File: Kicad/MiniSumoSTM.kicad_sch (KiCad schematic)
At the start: 0 parts

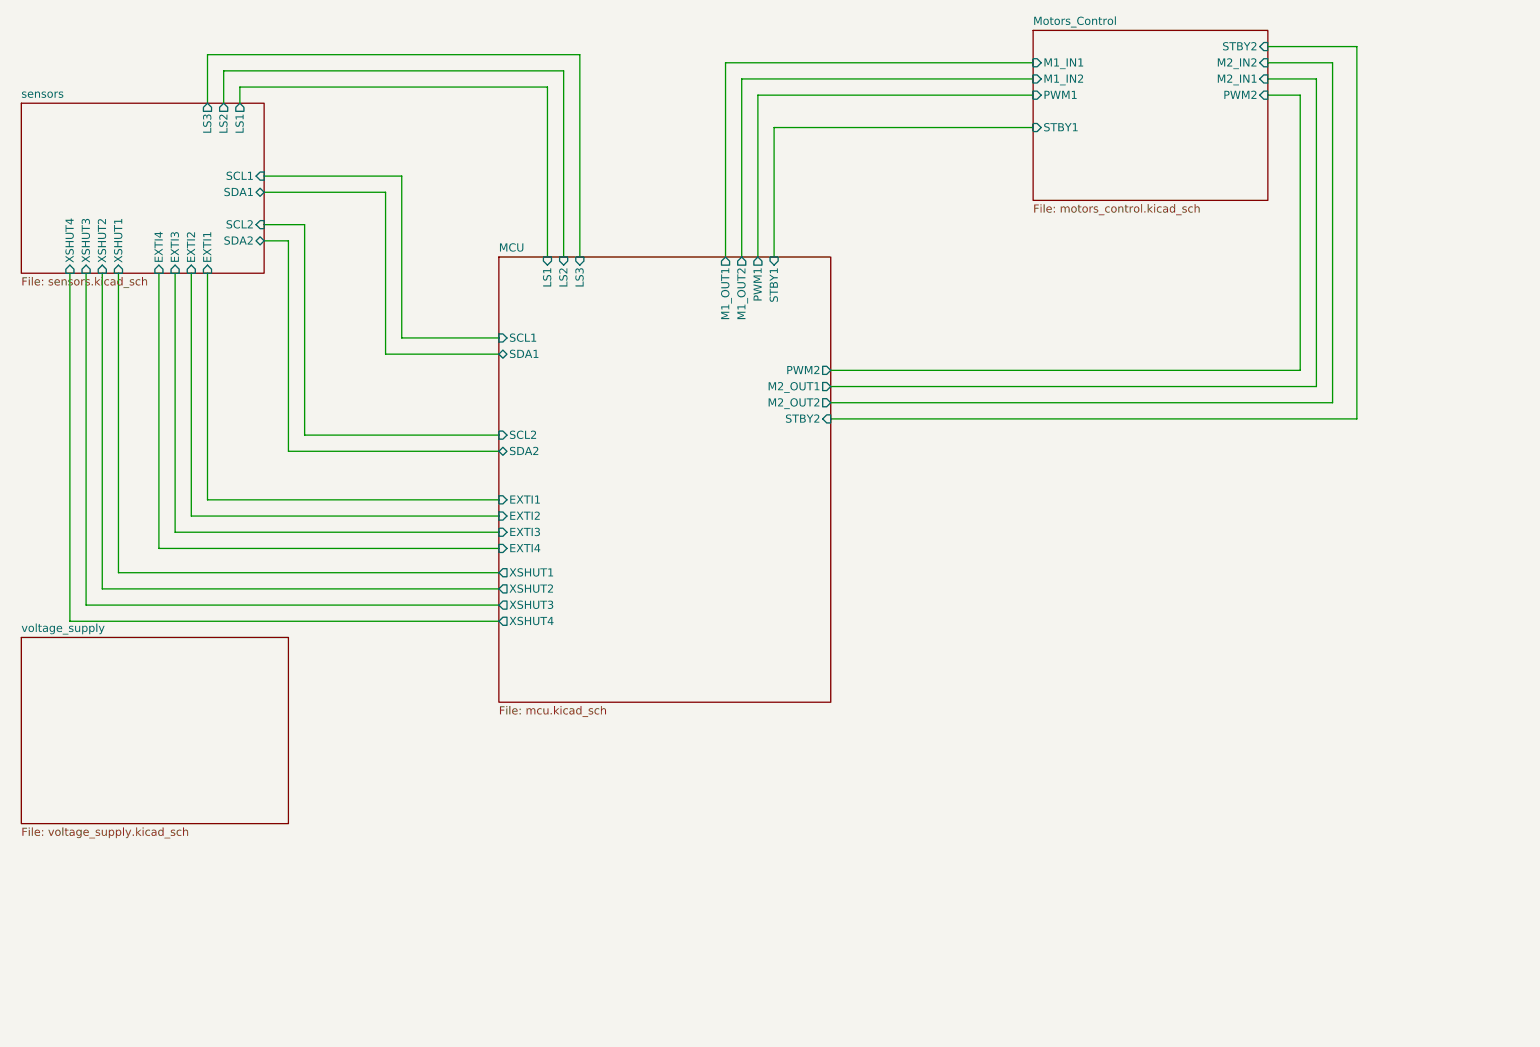
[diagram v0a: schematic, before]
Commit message: kicad schemas documentation
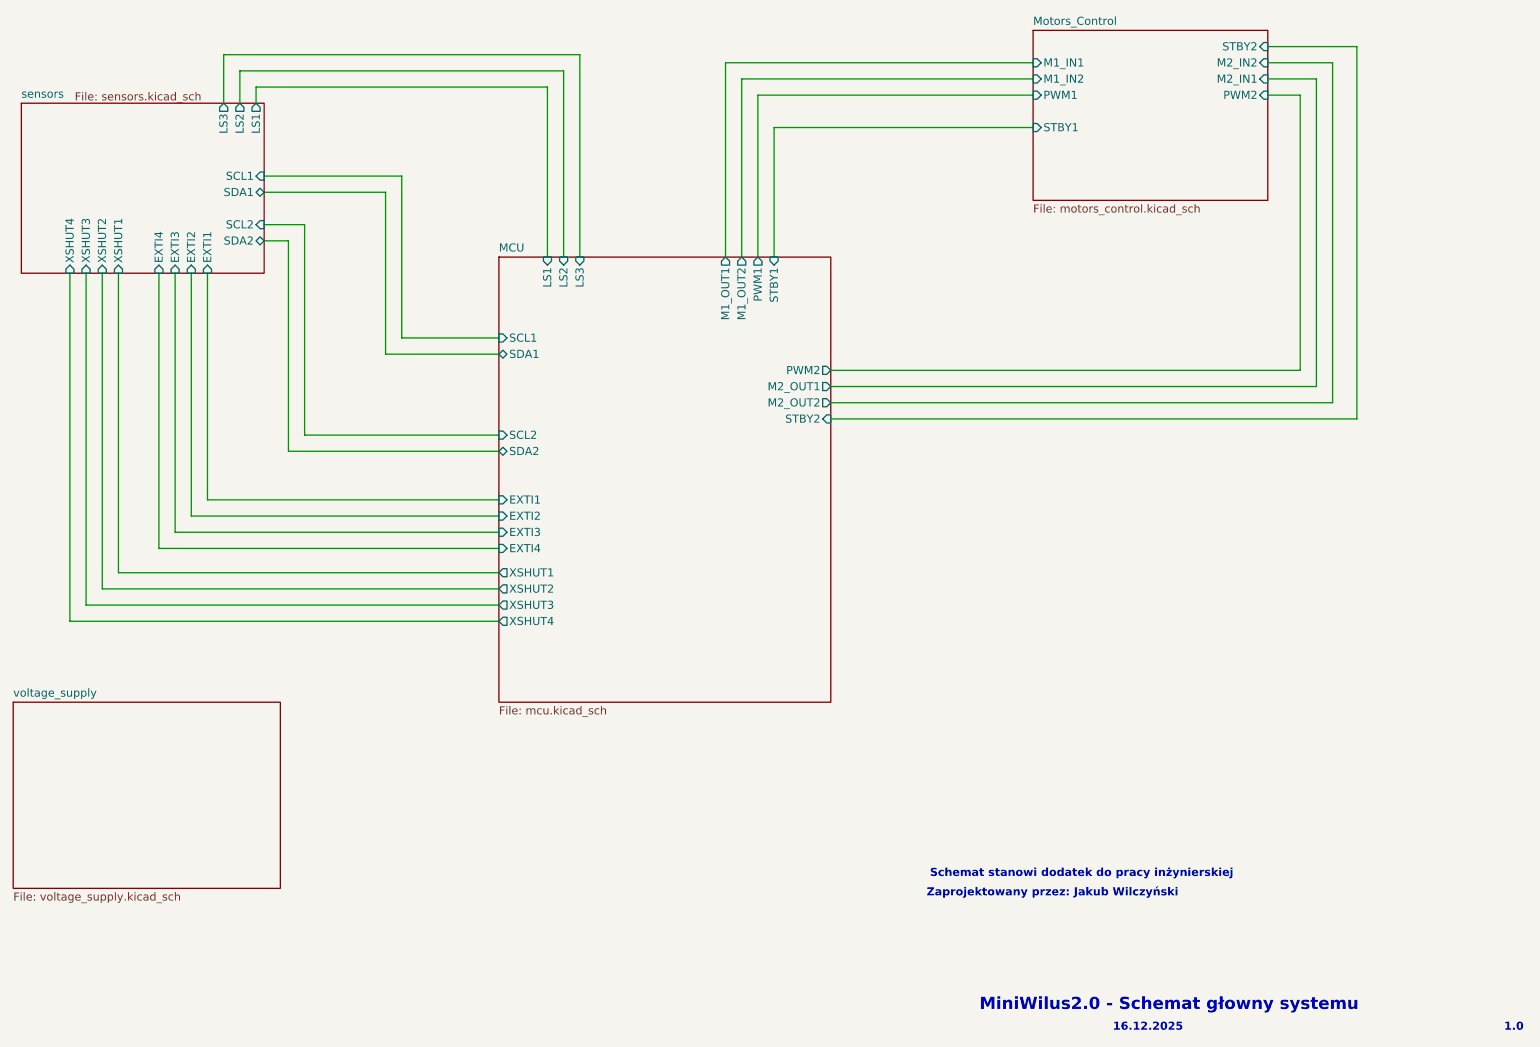
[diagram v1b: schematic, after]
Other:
- note added: "1.0"
- note added: "16.12.2025"
- note added: "MiniWilus2.0 - Schemat głowny systemu"
- note added: "Schemat stanowi dodatek do pracy inżynierskiej"
- note added: "Zaprojektowany przez: Jakub Wilczyński"
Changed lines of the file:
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@@
 	(generator_version "9.0")
 	(paper "A4")
+	(text "Zaprojektowany przez: Jakub Wilczyński"
+		(exclude_from_sim no)
+		(at 197.358 172.212 0)
+		(effects
+			(font
+				(size 1.27 1.27)
+				(thickness 0.254)
+				(bold yes)
+			)
+		)
+	)
+	(text "16.12.2025"
+		(exclude_from_sim no)
+		(at 212.344 193.294 0)
+		(effects
+			(font
+				(size 1.27 1.27)
+				(thickness 0.254)
+				(bold yes)
+			)
+		)
+	)
+	(text "MiniWilus2.0 - Schemat głowny systemu\n"
+		(exclude_from_sim no)
+		(at 215.646 189.738 0)
+		(effects
+			(font
+				(size 1.905 1.905)
+				(thickness 0.381)
+				(bold yes)
+			)
+		)
+	)
+	(text "Schemat stanowi dodatek do pracy inżynierskiej "
+		(exclude_from_sim no)
+		(at 201.93 169.164 0)
+		(effects
+			(font
+				(size 1.27 1.27)
+				(thickness 0.254)
+				(bold yes)
+			)
+		)
+	)
+	(text "1.0"
+		(exclude_from_sim no)
+		(at 269.748 193.294 0)
+		(effects
+			(font
+				(size 1.27 1.27)
+				(thickness 0.254)
+				(bold yes)
+			)
+		)
+	)
 	(wire
 		(pts
@@
 	(wire
 		(pts
-			(xy 64.77 40.64) (xy 64.77 48.26)
+			(xy 67.31 40.64) (xy 67.31 48.26)
 		)
 		(stroke
@@
 	(wire
 		(pts
-			(xy 67.31 43.18) (xy 67.31 48.26)
+			(xy 69.85 43.18) (xy 69.85 48.26)
 		)
 		(stroke
@@
 	(wire
 		(pts
-			(xy 69.85 45.72) (xy 69.85 48.26)
+			(xy 72.39 45.72) (xy 72.39 48.26)
 		)
 		(stroke
@@
 	(wire
 		(pts
-			(xy 118.11 45.72) (xy 69.85 45.72)
+			(xy 118.11 45.72) (xy 72.39 45.72)
 		)
 		(stroke
@@
 	(wire
 		(pts
-			(xy 123.19 40.64) (xy 64.77 40.64)
-		)
-		(stroke
-			(width 0)
-			(type default)
-		)
-	)
-	(wire
-		(pts
-			(xy 120.65 43.18) (xy 67.31 43.18)
+			(xy 123.19 40.64) (xy 67.31 40.64)
+		)
+		(stroke
+			(width 0)
+			(type default)
+		)
+	)
+	(wire
+		(pts
+			(xy 120.65 43.18) (xy 69.85 43.18)
 		)
 		(stroke
@@
 		(on_board yes)
 		(dnp no)
-		(fields_autoplaced yes)
 		(stroke
 			(width 0.1524)
@@
 		)
 		(property "Sheetfile" "sensors.kicad_sch"
-			(at 35.56 75.5146 0)
+			(at 43.942 46.482 0)
 			(effects
 				(font
@@
 		)
 		(pin "LS1" output
+			(at 72.39 48.26 90)
+			(effects
+				(font
+					(size 1.27 1.27)
+				)
+				(justify right)
+			)
+		)
+		(pin "LS2" output
 			(at 69.85 48.26 90)
 			(effects
@@
 			)
 		)
-		(pin "LS2" output
+		(pin "LS3" output
 			(at 67.31 48.26 90)
-			(effects
-				(font
-					(size 1.27 1.27)
-				)
-				(justify right)
-			)
-		)
-		(pin "LS3" output
-			(at 64.77 48.26 90)
 			(effects
 				(font
@@
 	)
 	(sheet
-		(at 35.56 132.08)
+		(at 34.29 142.24)
 		(size 41.91 29.21)
 		(exclude_from_sim no)
@@
 		)
 		(property "Sheetname" "voltage_supply"
-			(at 35.56 131.3684 0)
+			(at 34.29 141.5284 0)
 			(effects
 				(font
@@
 		)
 		(property "Sheetfile" "voltage_supply.kicad_sch"
-			(at 35.56 161.8746 0)
-			(effects
-				(font
+			(at 34.29 172.0346 0)
+			(effects
+				(font
